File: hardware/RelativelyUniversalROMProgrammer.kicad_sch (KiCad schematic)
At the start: 130 parts, among them J1 CTRL, J2 MSB, J3 LSB, J4 Ext_UART, J5 OLED, J6 VP, J7 SAO, J8 Conn_01x02, Q1 MMBT3904, Q10 MMBT3906, Q11 MMBT3904, Q12 MMBT3906, Q2 MMBT3906, Q3 MMBT3904, Q4 MMBT3904, Q5 MMBT3904, Q6 MMBT3906, Q7 MMBT3906, Q8 MMBT3906, Q9 MMBT3904, SW1 RST, SW2 USR, U1 MIC2288, U2 74HC573, U3 74HC573, U4 74HC573, U5 28/32 pin ROM

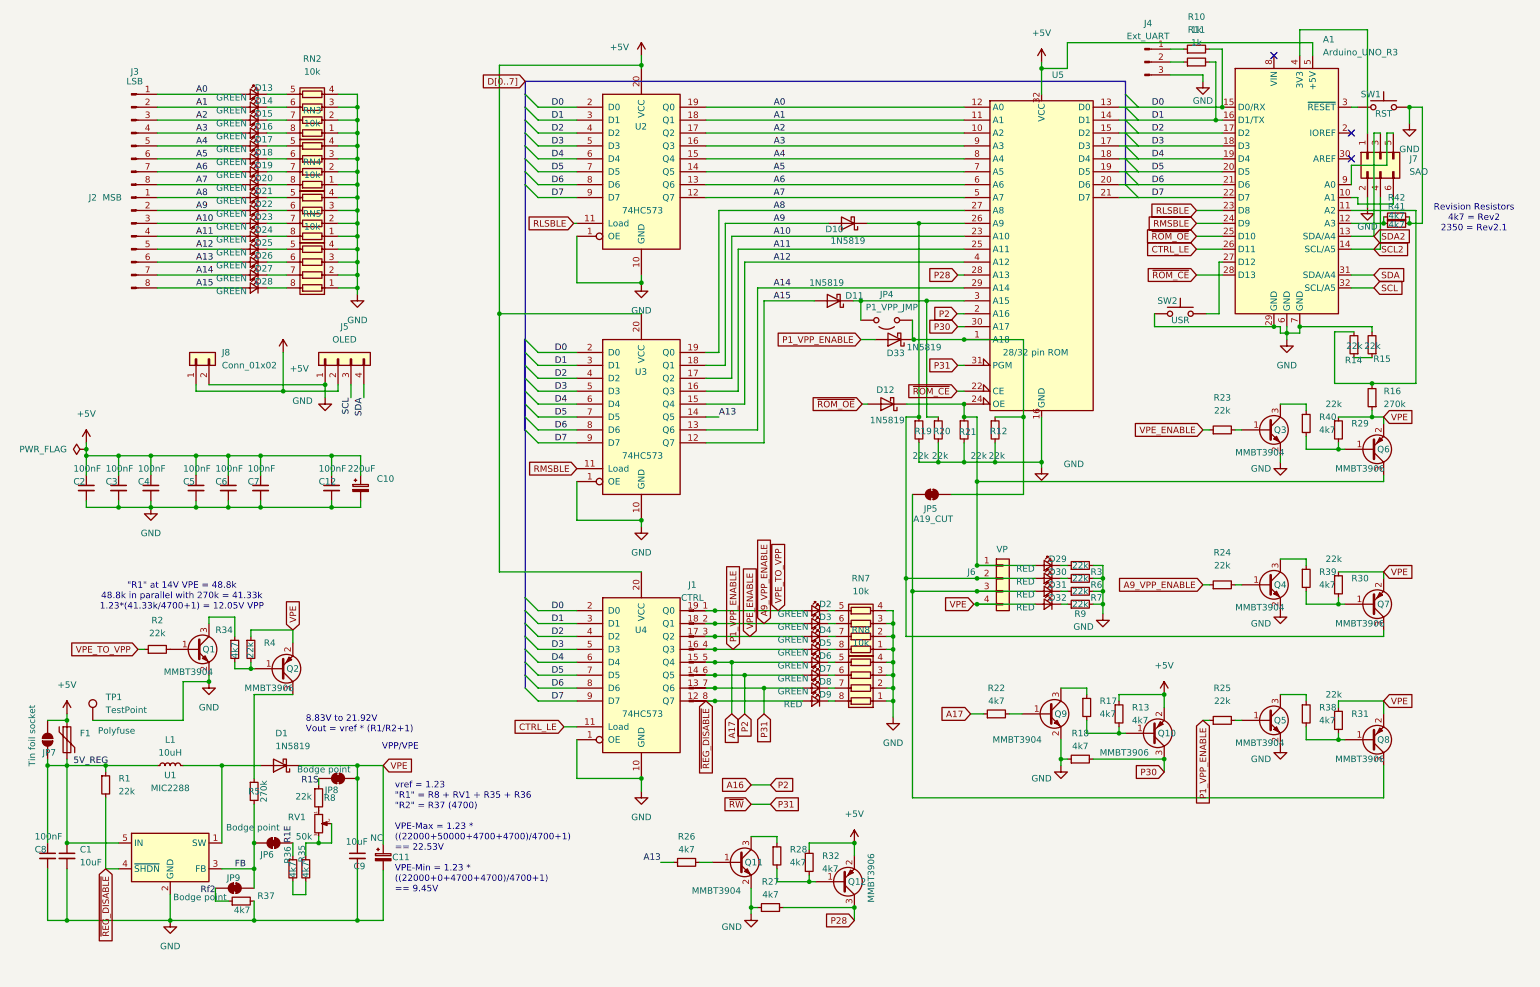
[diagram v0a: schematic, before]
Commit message: Rev 2.3
2716/2516 jumper
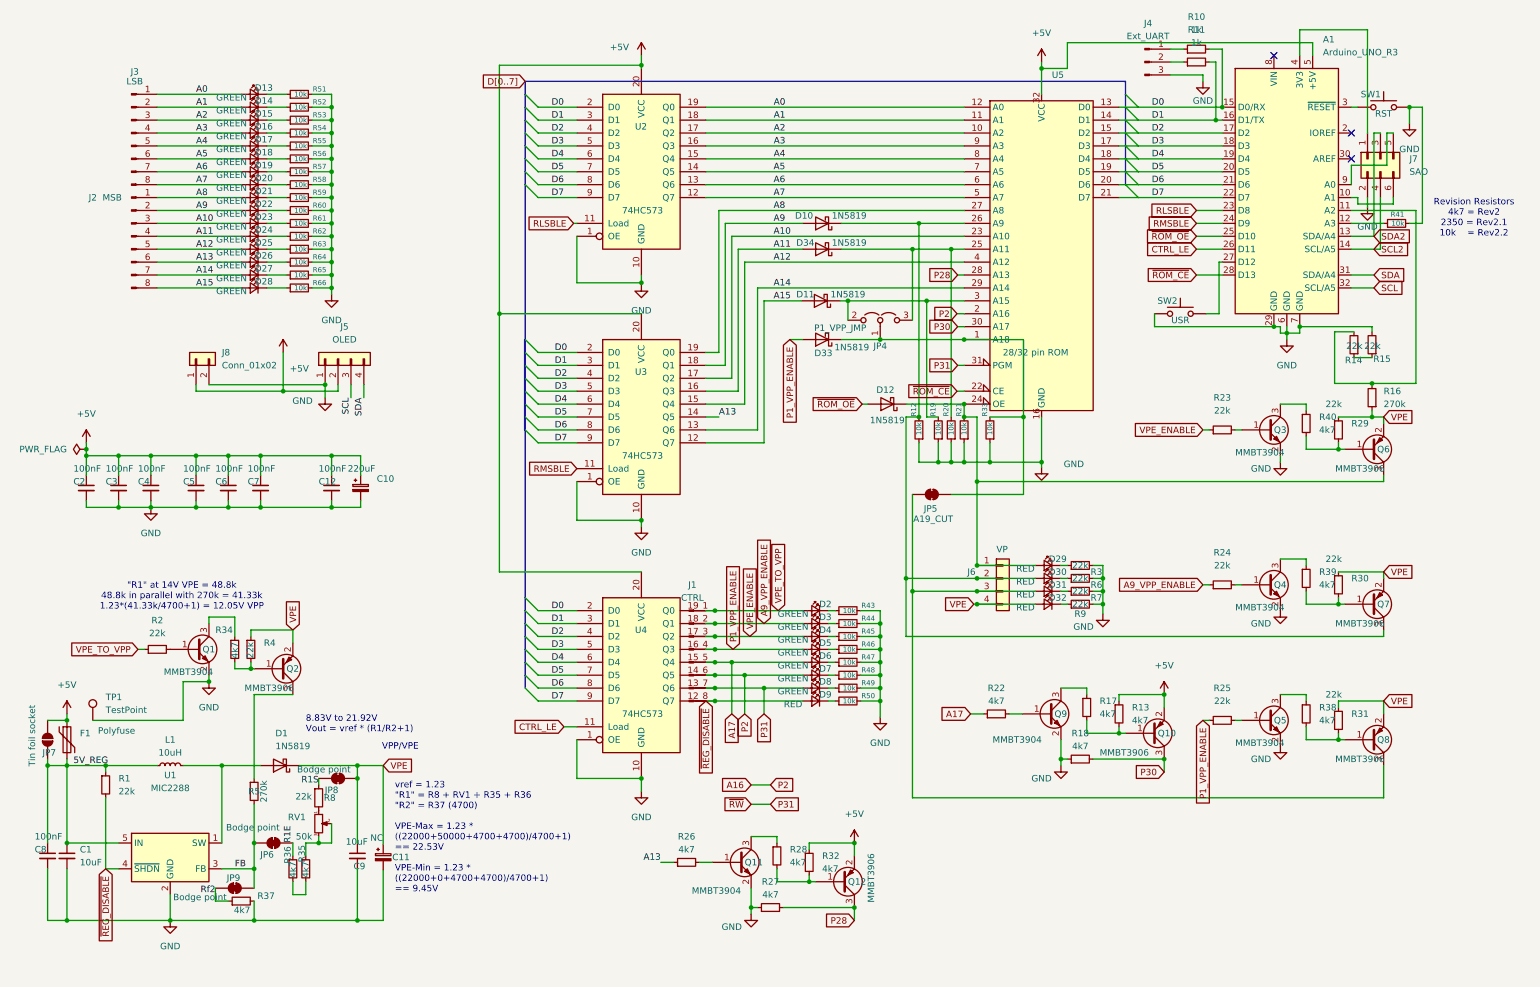
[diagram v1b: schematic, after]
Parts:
- removed R42: 4k7, Resistor_SMD:R_0402_1005Metric, symbol Device:R_Small
- removed RN2, RN3, RN4, RN5, RN7, RN8: 10k, Resistor_SMD:R_Array_Convex_4x0603, symbol Device:R_Pack04
- added D34: 1N5819, Diode_SMD:D_SOD-323, symbol Diode:1N5819
- added R33, R43, R44, R45, R46, R47, R48, R49, R50, R51, R52, R53, R54, R55, R56, R57, R58, R59, R60, R61, R62, R63, R64, R65, R66: 10k, Resistor_SMD:R_0402_1005Metric, symbol Device:R_Small
- JP4: footprint Connector_PinHeader_2.54mm:PinHeader_1x02_P2.54mm_Vertical -> Connector_PinHeader_2.54mm:PinHeader_2x02_P2.54mm_Vertical; symbol Jumper:Jumper_2_Open -> Jumper:Jumper_3_Open; now left out of the parts list
- R1, R14, R15, R2, R23, R24, R25, R29, R3, R30, R31, R4, R6, R7, R8, R9: LCSC (none) -> C31850
- R10, R11: LCSC (none) -> C21190
- R12, R19, R20, R21: value 22k -> 10k; footprint Resistor_SMD:R_0603_1608Metric -> Resistor_SMD:R_0402_1005Metric; LCSC (none) -> C25744
- R16, R5: LCSC (none) -> C22965
- R41: value 4k7 -> 10k; LCSC C25900 -> C25744
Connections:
- net A11: now also D34.2 (A); no longer U5.25 (A11)
- net GND: now also R12.1, R19.1, R20.1, R21.1, R33.1, R43.2, R44.2, R45.2, R46.2, R47.2, R48.2, R49.2, R50.2, R51.2, R52.2, R53.2, R54.2, R55.2, R56.2, R57.2, R58.2, R59.2, R60.2, R61.2, R62.2, R63.2, R64.2, R65.2, R66.2; no longer R12.2, R19.2, R20.2, R21.2
- net at D11.1 (K), JP4.2 (A), U5.3 (A15): now also R19.2; no longer R20.1
- net at D25.1 (K): now also R63.1
- net at D26.1 (K): now also R64.1
- net at D27.1 (K): now also R65.1
- net at D28.1 (K): now also R66.1
- net at D12.1 (K), D29.2 (A), J6.1 (Pin_1)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: now also R21.2; no longer R21.1
- net at D10.1 (K), D30.2 (A), J6.2 (Pin_2)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: now also R12.2; no longer R19.1
- net at D7.1 (K): now also R48.1
- net at D2.1 (K): now also R43.1
- net at D3.1 (K): now also R44.1
- net at D4.1 (K): now also R45.1
- net at D5.1 (K): now also R46.1
- net at D20.1 (K): now also R58.1
- net at D16.1 (K): now also R54.1
- net at D21.1 (K): now also R59.1
- net at D13.1 (K): now also R51.1
- net at D14.1 (K): now also R52.1
- net at D15.1 (K): now also R53.1
- net at D17.1 (K): now also R55.1
- net at D23.1 (K): now also R61.1
- net at D8.1 (K): now also R49.1
- net at D22.1 (K): now also R60.1
- net at D24.1 (K): now also R62.1
- net at D6.1 (K): now also R47.1
- net at D9.1 (K): now also R50.1
- net at D19.1 (K): now also R57.1
- net at D33.1 (K), JP4.1 (C), JP5.2 (B)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: now also R33.2; no longer R12.1
- net at D18.1 (K): now also R56.1
- new net: D34.1 (K), JP4.3 (B), R20.2, U5.25 (A11)
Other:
- note added: "Revision Resistors 4k7 = Rev2 2350 = Rev2.1 10k = Rev2.2"
- note removed: "Revision Resistors 4k7 = Rev2 2350 = Rev2.1"
- moved on the sheet: D10, D11, D33
